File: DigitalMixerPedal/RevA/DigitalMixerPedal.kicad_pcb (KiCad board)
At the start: 2 copper layers, 112.5 x 86.4 mm, 110 parts, among them J1 MonoJack2Switch, J2 MonoJack2Switch, J3 MonoJack2Switch, J4 MonoJack2Switch, J5 Barrel_Jack, J6 MonoJack2Switch, U1 TL072, U14 ISA0505, U15 MCP1754S-3302xCB, U16 TC593002ECB, U17 SE8250X2, U2 TL074, U3 TL072, U4 TL074, U5 TL072, U6 TL074, U7 TL072, U8 TL074, U9 TL072

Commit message: hw update
RevA layout completed (draft)
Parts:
- removed C48, C49, C50: 1uF, Capacitor_SMD:C_0805_2012Metric_Pad1.15x1.40mm_HandSolder
- removed the D1 at (137.5, 126.5)
- removed D10, D11, D12, D13, D7: 1N914, Diode_SMD:D_SOD-123F
- removed D6, D8: LED, LED_THT:LED_D5.0mm
- removed R19, R24: 220R, Resistor_SMD:R_0805_2012Metric_Pad1.15x1.40mm_HandSolder
- removed R22: 1K, Resistor_SMD:R_0805_2012Metric_Pad1.15x1.40mm_HandSolder
- removed R23: 10K, Resistor_SMD:R_0805_2012Metric_Pad1.15x1.40mm_HandSolder
- removed R25, R26, R27, R28: 10M, Resistor_SMD:R_0805_2012Metric_Pad1.15x1.40mm_HandSolder
- removed R29, R31, R32, R33: 100R, Resistor_SMD:R_0805_2012Metric_Pad1.15x1.40mm_HandSolder
- removed TP1, TP2, TP3, TP4: TestPoint, TestPoint:TestPoint_Pad_1.0x1.0mm
- removed U17: SE8250X2, Package_TO_SOT_SMD:SOT-23
- added C34: 100nF, Capacitor_SMD:C_0805_2012Metric_Pad1.15x1.40mm_HandSolder, F.Cu at (96.0, 95.1)
- added C35: 100nF, Capacitor_SMD:C_0805_2012Metric_Pad1.15x1.40mm_HandSolder, F.Cu at (73.9, 99.4)
- added C36: 100nF, Capacitor_SMD:C_0805_2012Metric_Pad1.15x1.40mm_HandSolder, F.Cu at (75.6, 95.0)
- added C37: 100nF, Capacitor_SMD:C_0805_2012Metric_Pad1.15x1.40mm_HandSolder, F.Cu at (135.5, 99.4)
- added C38: 100nF, Capacitor_SMD:C_0805_2012Metric_Pad1.15x1.40mm_HandSolder, F.Cu at (137.0, 95.1)
- added C39: 1uF, Capacitor_SMD:C_0805_2012Metric_Pad1.15x1.40mm_HandSolder, F.Cu at (51.9, 103.0)
- added C40: 1uF, Capacitor_SMD:C_0805_2012Metric_Pad1.15x1.40mm_HandSolder, F.Cu at (56.4, 108.1)
- added C41: 1uF, Capacitor_SMD:C_0805_2012Metric_Pad1.15x1.40mm_HandSolder, F.Cu at (125.2, 89.4)
- added C42: 1uF, Capacitor_SMD:C_0805_2012Metric_Pad1.15x1.40mm_HandSolder, F.Cu at (104.9, 89.4)
- added C43: 1uF, Capacitor_SMD:C_0805_2012Metric_Pad1.15x1.40mm_HandSolder, F.Cu at (84.2, 89.4)
- added C44: 1uF, Capacitor_SMD:C_0805_2012Metric_Pad1.15x1.40mm_HandSolder, F.Cu at (63.8, 89.3)
- added C45: 1uF, Capacitor_SMD:C_0805_2012Metric_Pad1.15x1.40mm_HandSolder, F.Cu at (48.1, 108.1)
- added J7: Conn_01x05, Connector_PinHeader_2.54mm:PinHeader_1x05_P2.54mm_Vertical, F.Cu at (103.8, 127.8)
- added JP1: Jumper_NO_Small, Jumper:SolderJumper-2_P1.3mm_Open_Pad1.0x1.5mm, F.Cu at (54.9, 95.8)
- added U10: TPS60400, Package_TO_SOT_SMD:SOT-23-5_HandSoldering, F.Cu at (67.6, 89.3)
- added U11: STM32F051K8Tx, Package_QFP:LQFP-32_7x7mm_P0.8mm, F.Cu at (98.4, 120.1)
- added U12: MCP601-xOT, Package_TO_SOT_SMD:SOT-23-5, F.Cu at (115.3, 103.3)
- added U13: MCP601-xOT, Package_TO_SOT_SMD:SOT-23-5, F.Cu at (94.4, 103.4)
- C1, C10, C11, C12, C16, C17, C18, C2, C22, C23, C24, C28, C29, C3, C4, C5, C6, J1, J2, J3, J4, J5, J6, R1, R10, R11, R15, R16, R2, R20, R21, R3, R30, R4, R5, R6, U1, U3, U5, U7, U9: moved to F.Cu
- C13, C14, C15, C19, C7, C8, C9: value 100nF -> 1uF; moved to F.Cu
- C20: value 100nF -> 1uF; footprint Capacitor_SMD:C_0805_2012Metric_Pad1.15x1.40mm_HandSolder -> Capacitor_SMD:C_1206_3216Metric_Pad1.42x1.75mm_HandSolder; moved to F.Cu
- C21: footprint Capacitor_SMD:C_0805_2012Metric_Pad1.15x1.40mm_HandSolder -> Capacitor_SMD:C_1206_3216Metric_Pad1.42x1.75mm_HandSolder; moved to F.Cu
- C25: value 100nF -> 1uF
- C30: value 1nF -> 100nF
- C31, C32, C33: value 1nF -> 100nF; moved to F.Cu
- D1: renamed from D9; moved to F.Cu
- D2, D4, RV1, RV2, RV3, RV4: moved to B.Cu
- D3, D5: value 1N914 -> LED; footprint Diode_SMD:D_SOD-123F -> LED_THT:LED_D5.0mm
- R12, R7: value 1K -> R
- R13, R18: value 10K -> 50R; moved to F.Cu
- R14: value 220R -> 50R; moved to F.Cu
- R17: value 1K -> 50R; moved to F.Cu
- R8: value 10K -> R
- R9: value 220R -> R
- U14: value ISA0505 -> MCP601-xOT; footprint XP_ISA:ISA0505 -> Package_TO_SOT_SMD:SOT-23-5; moved to F.Cu
- U15: value MCP1754S-3302xCB -> MCP601-xOT; footprint Package_TO_SOT_SMD:SOT-23 -> Package_TO_SOT_SMD:SOT-23-5; moved to F.Cu
- U16: value TC593002ECB -> TPS60400; footprint Package_TO_SOT_SMD:SOT-23 -> Package_TO_SOT_SMD:SOT-23-5_HandSoldering; moved to F.Cu
- U2: value TL074 -> MCP1703A-3302_SOT223; footprint Package_SO:SOIC-14_3.9x8.7mm_P1.27mm -> Package_TO_SOT_SMD:SOT-223-3_TabPin2; moved to F.Cu
- U4, U6, U8: value TL074 -> TPS60400; footprint Package_SO:SOIC-14_3.9x8.7mm_P1.27mm -> Package_TO_SOT_SMD:SOT-23-5_HandSoldering; moved to F.Cu
- moved U2 93.2 mm to (50.8, 88.9)
- moved R7 84.4 mm to (65.3, 58.9), turned to 0 degrees
- moved U15 77.6 mm to (135.5, 103.3)
- moved D5 74.1 mm to (129.3, 62.7), turned to 270 degrees
- moved R9 73.0 mm to (106.4, 58.9), turned to 0 degrees
- moved R8 70.1 mm to (85.9, 58.9), turned to 0 degrees
- moved C3 69.9 mm to (129.2, 85.6), turned to 0 degrees
- moved D3 68.9 mm to (88.1, 62.7), turned to 270 degrees
- moved C15 65.5 mm to (67.6, 85.5)
- moved D2 61.8 mm to (67.6, 62.7), turned to 270 degrees
- moved C21 55.0 mm to (50.8, 96.5), turned to 270 degrees
- moved C20 52.1 mm to (50.8, 81.3)
- moved R12 49.0 mm to (127.0, 58.9), turned to 0 degrees
- moved C9 48.7 mm to (112.5, 89.4), turned to 270 degrees
- moved R18 42.9 mm to (134.5, 95.1), turned to 270 degrees
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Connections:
- C1 pad 1: /PowerSupply/+9V_POL -> Net-(C1-Pad1)
- C10 pad 1: -3V3 -> /InputBuffer2/NEG3VIN
- C10 pad 2: VCOM -> GNDS
- C11 pad 2: VCOM -> GNDS
- C12 pad 1: /PeakDetector2/SIGNAL_INPUT -> /PEAK_IN_BUF2
- C13 pad 1: +3V3 -> Net-(C13-Pad1)
- C13 pad 2: VCOM -> Net-(C13-Pad2)
- C14 pad 1: -3V3 -> /InputBuffer3/NEG3VIN
- C14 pad 2: VCOM -> GNDS
- C15 pad 2: VCOM -> Net-(C15-Pad2)
- C16 pad 1: -3V3 -> /InputBuffer3/NEG3VIN
- C16 pad 2: VCOM -> GNDS
- C17 pad 2: VCOM -> GNDS
- C18 pad 1: /PeakDetector3/SIGNAL_INPUT -> /PEAK_IN_BUF3
- C19 pad 1: +3V3 -> /InputBuffer4/NEG3VIN
- C19 pad 2: VCOM -> GNDS
- C2 pad 1: /PowerSupply/+5V_REG -> Net-(C2-Pad1)
- C20 pad 1: -3V3 -> Net-(C1-Pad1)
- C20 pad 2: VCOM -> GNDS
- C21 pad 1: Net-(C21-Pad1) -> Net-(C2-Pad1)
- C21 pad 2: VCOM -> GNDS
- C22 pad 1: -3V3 -> /InputBuffer4/NEG3VIN
- C22 pad 2: VCOM -> GNDS
- C23 pad 2: VCOM -> GNDS
- C24 pad 1: /PeakDetector4/SIGNAL_INPUT -> /PEAK_IN_BUF4
- C25 pad 2: VCOM -> GNDS
- C26 pad 1: -3V3 -> +3V3
- C26 pad 2: VCOM -> GNDS
- C27 pad 1: Net-(C27-Pad1) -> +3V3
- C27 pad 2: VCOM -> GNDS
- C28 pad 1: -3V3 -> /OutputStage/NEG3VIN
- C28 pad 2: VCOM -> GNDS
- C29 pad 2: VCOM -> GNDS
- C3 pad 2: VCOM -> Net-(C3-Pad2)
- C30 pad 1: Net-(C30-Pad1) -> +3V3
- C30 pad 2: Net-(C30-Pad2) -> GNDS
- C31 pad 1: Net-(C31-Pad1) -> +3V3
- C31 pad 2: Net-(C31-Pad2) -> GNDS
- C32 pad 1: Net-(C32-Pad1) -> /PeakDetectorMCU/PEAK_IN_ADC2
- C32 pad 2: Net-(C32-Pad2) -> GNDS
- C33 pad 1: Net-(C33-Pad1) -> +3V3
- C33 pad 2: Net-(C33-Pad2) -> GNDS
- C4 pad 1: -3V3 -> /InputBuffer1/NEG3VIN
- C4 pad 2: VCOM -> GNDS
- C5 pad 2: VCOM -> GNDS
- C6 pad 1: /PeakDetector1/SIGNAL_INPUT -> /PEAK_IN_BUF1
- C7 pad 1: +3V3 -> /InputBuffer1/NEG3VIN
- C7 pad 2: VCOM -> GNDS
- C8 pad 1: -3V3 -> Net-(C8-Pad1)
- C8 pad 2: VCOM -> Net-(C8-Pad2)
- C9 pad 1: Net-(C9-Pad1) -> /InputBuffer2/NEG3VIN
- C9 pad 2: VCOM -> GNDS
- D1 pad 1: /PowerSupply/+9V_POL -> Net-(C1-Pad1)
- D2 pad 1: VCOM -> Net-(D2-Pad1)
- D2 pad 2: Net-(D2-Pad2) -> /PeakDetectorMCU/PEAK_OUT_PWM4
- D3 pad 1: Net-(C15-Pad1) -> Net-(D3-Pad1)
- D3 pad 2: Net-(C31-Pad1) -> /PeakDetectorMCU/PEAK_OUT_PWM3
- D4 pad 1: VCOM -> Net-(D4-Pad1)
- D4 pad 2: Net-(D4-Pad2) -> /PeakDetectorMCU/PEAK_OUT_PWM2
- D5 pad 1: Net-(C21-Pad1) -> Net-(D5-Pad1)
- D5 pad 2: Net-(C32-Pad1) -> /PeakDetectorMCU/PEAK_OUT_PWM1
- J1 pad 2: Net-(J1-Pad2) -> GNDS
- J1 pad 3: VCOM -> GNDS
- J1 pad 4: VCOM -> GNDS
- J2 pad 2: Net-(J2-Pad2) -> GNDS
- J2 pad 3: VCOM -> GNDS
- J2 pad 4: VCOM -> GNDS
- J3 pad 2: Net-(J3-Pad2) -> GNDS
- J3 pad 3: VCOM -> GNDS
- J3 pad 4: VCOM -> GNDS
- J4 pad 2: Net-(J4-Pad2) -> GNDS
- J4 pad 3: VCOM -> GNDS
- J4 pad 4: VCOM -> GNDS
- J6 pad 2: VCOM -> GNDS
- J6 pad 3: VCOM -> GNDS
- J6 pad 4: VCOM -> GNDS
- R1 pad 2: /PeakDetector1/SIGNAL_INPUT -> /PEAK_IN_BUF1
- R11 pad 1: /PeakDetector2/SIGNAL_INPUT -> /PEAK_IN_BUF2
- R12 pad 1: VCOM -> GNDS
- R12 pad 2: Net-(R12-Pad2) -> Net-(D5-Pad1)
- R13 pad 1: Net-(R12-Pad2) -> /PeakDetectorMCU/PEAK_IN_ADC2
- R14 pad 1: Net-(D4-Pad2) -> /PeakDetectorMCU/PEAK_IN_ADC3
- R16 pad 1: /PeakDetector3/SIGNAL_INPUT -> /PEAK_IN_BUF3
- R17 pad 1: VCOM -> /PeakDetectorMCU/PEAK_IN_ADC4
- R18 pad 1: Net-(R17-Pad2) -> /PeakDetectorMCU/PEAK_IN_ADC1
- R2 pad 2: /PeakDetector2/SIGNAL_INPUT -> /PEAK_IN_BUF2
- R21 pad 1: /PeakDetector4/SIGNAL_INPUT -> /PEAK_IN_BUF4
- R3 pad 2: /PeakDetector3/SIGNAL_INPUT -> /PEAK_IN_BUF3
- R4 pad 2: /PeakDetector4/SIGNAL_INPUT -> /PEAK_IN_BUF4
- R6 pad 1: /PeakDetector1/SIGNAL_INPUT -> /PEAK_IN_BUF1
- R7 pad 1: VCOM -> GNDS
- R7 pad 2: Net-(R7-Pad2) -> Net-(D2-Pad1)
- R8 pad 1: Net-(R7-Pad2) -> GNDS
- R8 pad 2: Net-(R8-Pad2) -> Net-(D3-Pad1)
- R9 pad 1: Net-(D2-Pad2) -> GNDS
- R9 pad 2: Net-(R9-Pad2) -> Net-(D4-Pad1)
- U1 pad 4: -3V3 -> /InputBuffer1/NEG3VIN
- U1 pad 5: VCOM -> GNDS
- U1 pad 7: /PeakDetector1/SIGNAL_INPUT -> /PEAK_IN_BUF1
- U14 pad 1: GNDS -> Net-(R17-Pad2)
- U14 pad 2: /PowerSupply/+5V_REG -> GNDS
- U14 pad 4: VCOM -> Net-(R17-Pad2)
- U14 pad 5: Net-(C48-Pad2) -> +3V3
- U15 pad 1: VCOM -> Net-(R18-Pad2)
- U15 pad 2: +3V3 -> GNDS
- U15 pad 3: Net-(C3-Pad1) -> /PEAK_IN_BUF1
- U16 pad 1: -3V3 -> /OutputStage/NEG3VIN
- U16 pad 2: Net-(C48-Pad2) -> +3V3
- U16 pad 3: VCOM -> Net-(C39-Pad1)
- U2 pad 1: Net-(C30-Pad1) -> Net-(C1-Pad1)
- U2 pad 2: Net-(C30-Pad2) -> GNDS
- U2 pad 3: Net-(R8-Pad2) -> Net-(C2-Pad1)
- U3 pad 4: -3V3 -> /InputBuffer2/NEG3VIN
- U3 pad 5: VCOM -> GNDS
- U3 pad 7: /PeakDetector2/SIGNAL_INPUT -> /PEAK_IN_BUF2
- U4 pad 1: Net-(C31-Pad1) -> /InputBuffer1/NEG3VIN
- U4 pad 2: Net-(C31-Pad2) -> +3V3
- U4 pad 3: Net-(R13-Pad2) -> Net-(C3-Pad1)
- U4 pad 4: +3V3 -> GNDS
- U4 pad 5: /PeakDetector2/SIGNAL_INPUT -> Net-(C3-Pad2)
- U5 pad 4: -3V3 -> /InputBuffer3/NEG3VIN
- U5 pad 5: VCOM -> GNDS
- U5 pad 7: /PeakDetector3/SIGNAL_INPUT -> /PEAK_IN_BUF3
- U6 pad 1: Net-(C32-Pad1) -> /InputBuffer2/NEG3VIN
- U6 pad 2: Net-(C32-Pad2) -> +3V3
- U6 pad 3: Net-(R18-Pad2) -> Net-(C8-Pad1)
- U6 pad 4: +3V3 -> GNDS
- U6 pad 5: /PeakDetector3/SIGNAL_INPUT -> Net-(C8-Pad2)
- U7 pad 4: -3V3 -> /InputBuffer4/NEG3VIN
- U7 pad 5: VCOM -> GNDS
- U7 pad 7: /PeakDetector4/SIGNAL_INPUT -> /PEAK_IN_BUF4
- U8 pad 1: Net-(C33-Pad1) -> /InputBuffer3/NEG3VIN
- U8 pad 2: Net-(C33-Pad2) -> +3V3
- U8 pad 3: Net-(R23-Pad2) -> Net-(C13-Pad1)
- U8 pad 4: +3V3 -> GNDS
- U8 pad 5: /PeakDetector4/SIGNAL_INPUT -> Net-(C13-Pad2)
- U9 pad 3: VCOM -> GNDS
- U9 pad 4: -3V3 -> /OutputStage/NEG3VIN
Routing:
- net -3V3: track 473.8 -> 0.00 mm, vias 14 -> 0
- net +3V3: track 471.8 -> 299.6 mm, vias 16 -> 15
- net VCOM: track 134.4 -> 0.00 mm, vias 29 -> 0
- net /PeakDetectorMCU/PEAK_OUT_PWM1: track 0.00 -> 93.9 mm
- net /PeakDetectorMCU/PEAK_OUT_PWM3: track 0.00 -> 79.6 mm, vias 0 -> 2
- net Net-(D2-Pad2): track 77.7 -> 0.00 mm, vias 2 -> 0
- net Net-(D4-Pad2): track 75.8 -> 0.00 mm, vias 2 -> 0
- net /PeakDetectorMCU/PEAK_OUT_PWM4: track 0.00 -> 74.9 mm, vias 0 -> 2
- net Net-(D6-Pad2): track 74.3 -> 0.00 mm, vias 2 -> 0
- net Net-(D8-Pad2): track 73.9 -> 0.00 mm, vias 2 -> 0
- net /PeakDetectorMCU/PEAK_OUT_PWM2: track 0.00 -> 73.8 mm, vias 0 -> 2
- net /PeakDetectorMCU/PEAK_IN_ADC1: track 0.00 -> 66.7 mm
- net GNDS: track 43.1 -> 106.3 mm, vias 0 -> 56
- net /OutputStage/SIGNAL_INPUT: track 154.4 -> 96.7 mm, vias 0 -> 10
- net /PeakDetector1/SIGNAL_INPUT: track 51.9 -> 0.00 mm
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- added copper zone on B.Cu, net GNDS
- added copper zone on F.Cu, net GNDS
- removed copper zone on F.Cu, net VCOM

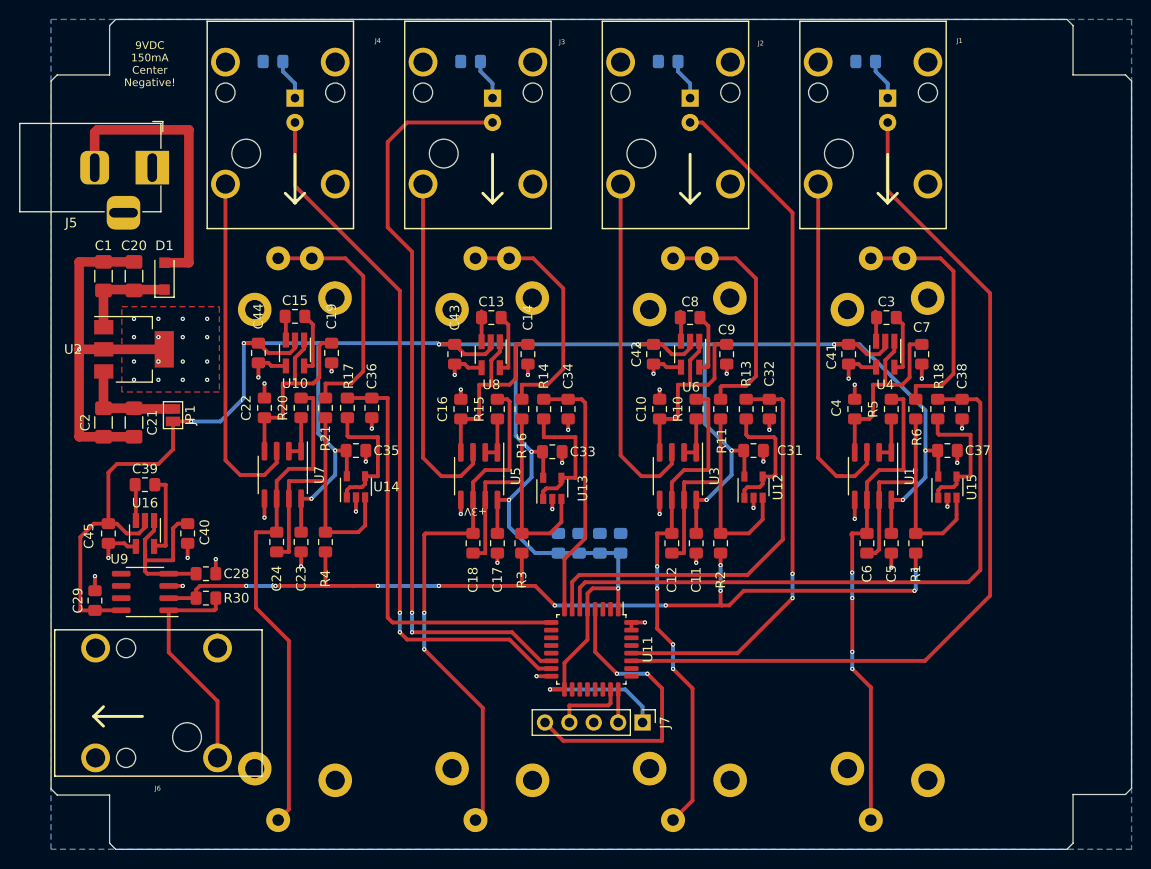
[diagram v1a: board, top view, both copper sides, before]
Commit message: updated hw
- added testpoints
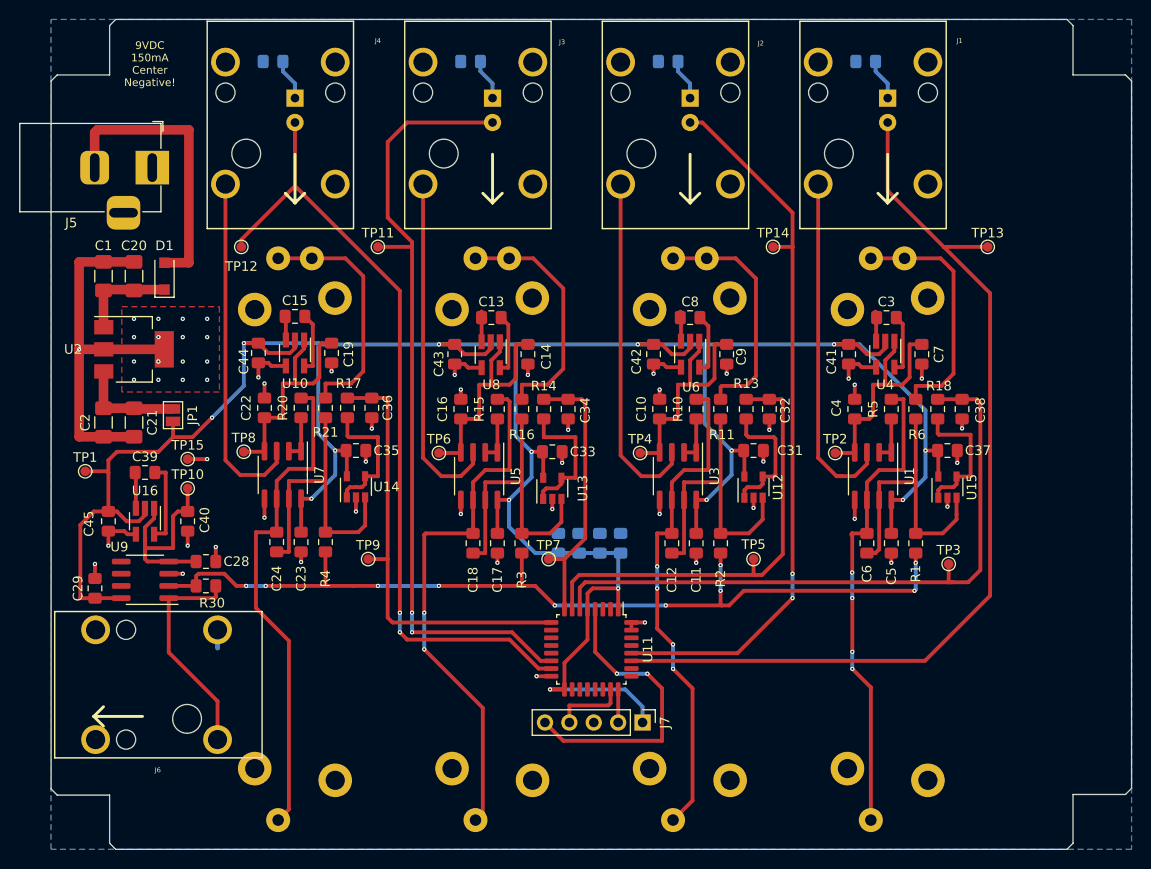
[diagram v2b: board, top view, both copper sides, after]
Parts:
- added TP1: TestPoint, TestPoint:TestPoint_Pad_D1.0mm, F.Cu at (45.7, 101.6)
- added TP10: TestPoint, TestPoint:TestPoint_Pad_D1.0mm, F.Cu at (56.4, 103.4)
- added TP11: TestPoint, TestPoint:TestPoint_Pad_D1.0mm, F.Cu at (76.2, 78.2)
- added TP12: TestPoint, TestPoint:TestPoint_Pad_D1.0mm, F.Cu at (62.0, 78.2)
- added TP13: TestPoint, TestPoint:TestPoint_Pad_D1.0mm, F.Cu at (139.7, 78.2)
- added TP14: TestPoint, TestPoint:TestPoint_Pad_D1.0mm, F.Cu at (117.3, 78.2)
- added TP15: TestPoint, TestPoint:TestPoint_Pad_D1.0mm, F.Cu at (56.4, 100.3)
- added TP2: TestPoint, TestPoint:TestPoint_Pad_D1.0mm, F.Cu at (123.8, 99.7)
- added TP3: TestPoint, TestPoint:TestPoint_Pad_D1.0mm, F.Cu at (135.6, 111.3)
- added TP4: TestPoint, TestPoint:TestPoint_Pad_D1.0mm, F.Cu at (103.5, 99.7)
- added TP5: TestPoint, TestPoint:TestPoint_Pad_D1.0mm, F.Cu at (115.3, 110.7)
- added TP6: TestPoint, TestPoint:TestPoint_Pad_D1.0mm, F.Cu at (82.5, 99.7)
- added TP7: TestPoint, TestPoint:TestPoint_Pad_D1.0mm, F.Cu at (94.0, 110.7)
- added TP8: TestPoint, TestPoint:TestPoint_Pad_D1.0mm, F.Cu at (62.2, 99.6)
- added TP9: TestPoint, TestPoint:TestPoint_Pad_D1.0mm, F.Cu at (75.2, 110.7)
- moved J6 1.91 mm to (53.3, 123.8)
- moved R30 1.27 mm to (58.3, 113.5)
- moved C28 1.27 mm to (58.3, 111.0)
- moved C29 1.27 mm to (46.7, 113.8)
- moved C39 1.27 mm to (51.9, 101.7)
- moved C40 1.27 mm to (56.4, 106.8)
- moved C45 1.27 mm to (48.1, 106.8)
- moved U16 1.27 mm to (51.9, 106.8)
- moved U9 1.27 mm to (51.9, 112.9)
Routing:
- net /PeakDetectorMCU/PEAK_OUT_PWM4: track 74.9 -> 83.6 mm
- net /PeakDetectorMCU/PEAK_OUT_PWM1: track 93.9 -> 98.4 mm
- net /PeakDetectorMCU/PEAK_OUT_PWM3: track 79.6 -> 83.2 mm
- net /PeakDetectorMCU/PEAK_IN_ADC2: track 45.0 -> 47.6 mm
- net /PeakDetectorMCU/PEAK_IN_ADC1: track 66.7 -> 69.2 mm
- net /OutputStage/NEG3VIN: track 20.1 -> 22.5 mm
- net /InputBuffer4/NEG3VIN: track 22.6 -> 25.0 mm
- net /InputBuffer3/NEG3VIN: track 22.7 -> 25.0 mm
- net /InputBuffer2/NEG3VIN: track 22.6 -> 24.7 mm
- net /InputBuffer1/NEG3VIN: track 22.5 -> 24.5 mm
- net /PeakDetectorMCU/PEAK_OUT_PWM2: track 73.8 -> 75.9 mm
- net /PeakDetectorMCU/PEAK_IN_ADC4: track 44.3 -> 46.3 mm
- net /PeakDetectorMCU/PEAK_IN_ADC3: track 26.9 -> 28.5 mm
- net +3V3: track 299.6 -> 300.8 mm
- net GNDS: track 106.3 -> 107.4 mm, vias 56 -> 57
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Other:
- board text added: "4-Way Mixer with Digital Peak Detect RevA 3920"
- board text removed: "+3V"
- board text removed: "Active 4-way Mixer RevC 3720"
